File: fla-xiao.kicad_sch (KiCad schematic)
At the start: 9 parts, among them J1 Conn_PinHeader_1x08_P2.54mm_V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, J2 Conn_PinHeader_1x04_P2.54mm_V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, J3 Conn_PinHeader_2x03_P2.54mm_V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, SW1 BUTTON_B3SN, U1 MOUDLE-SEEEDUINO-XIAO-ESP32C3

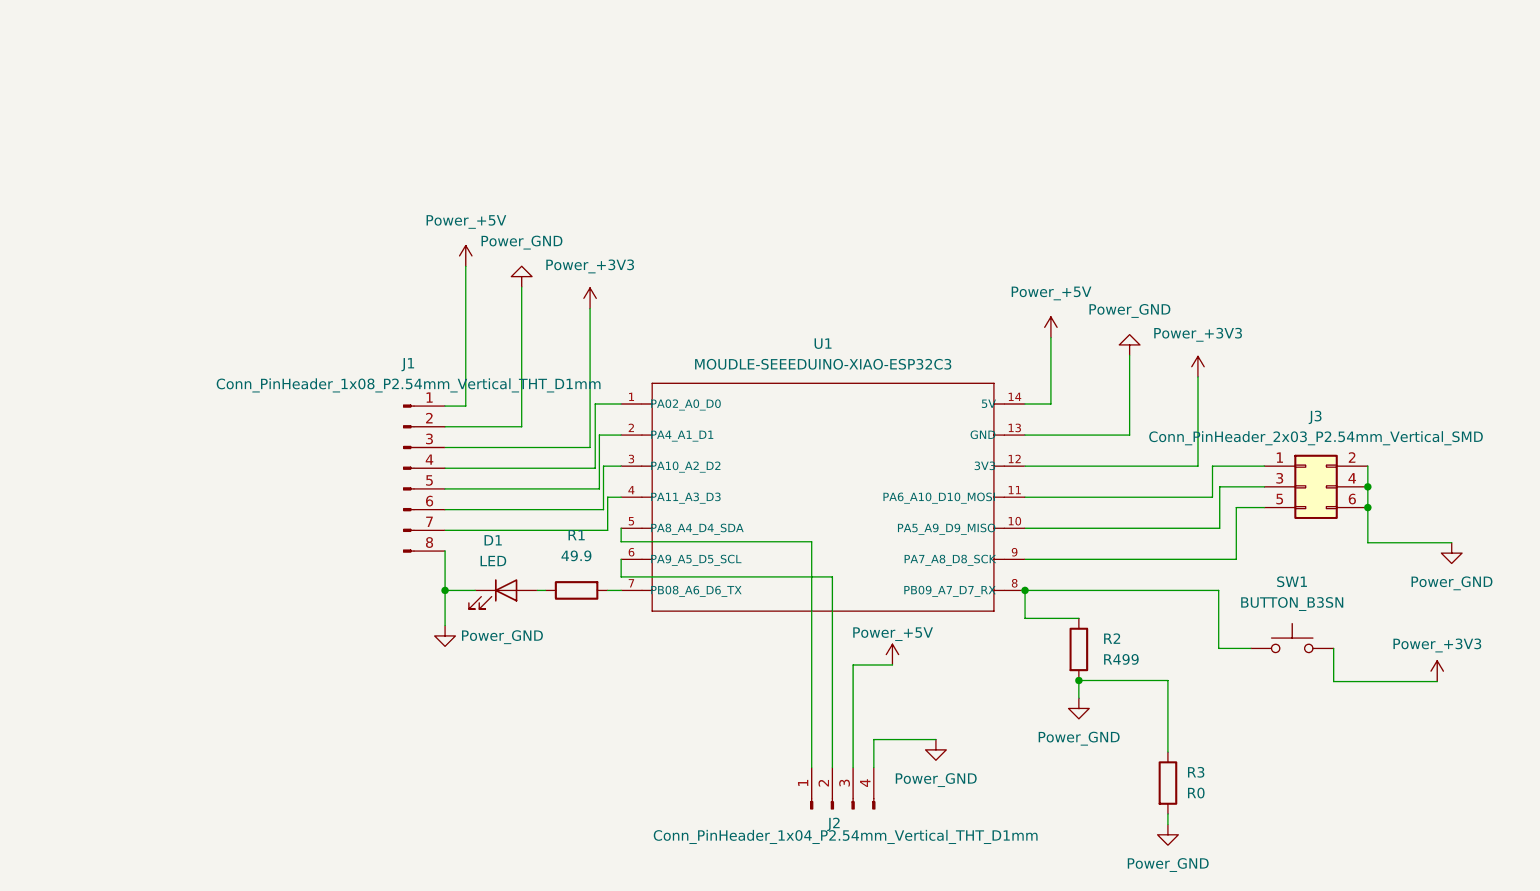
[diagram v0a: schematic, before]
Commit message: Updated to use sockets with XIAO
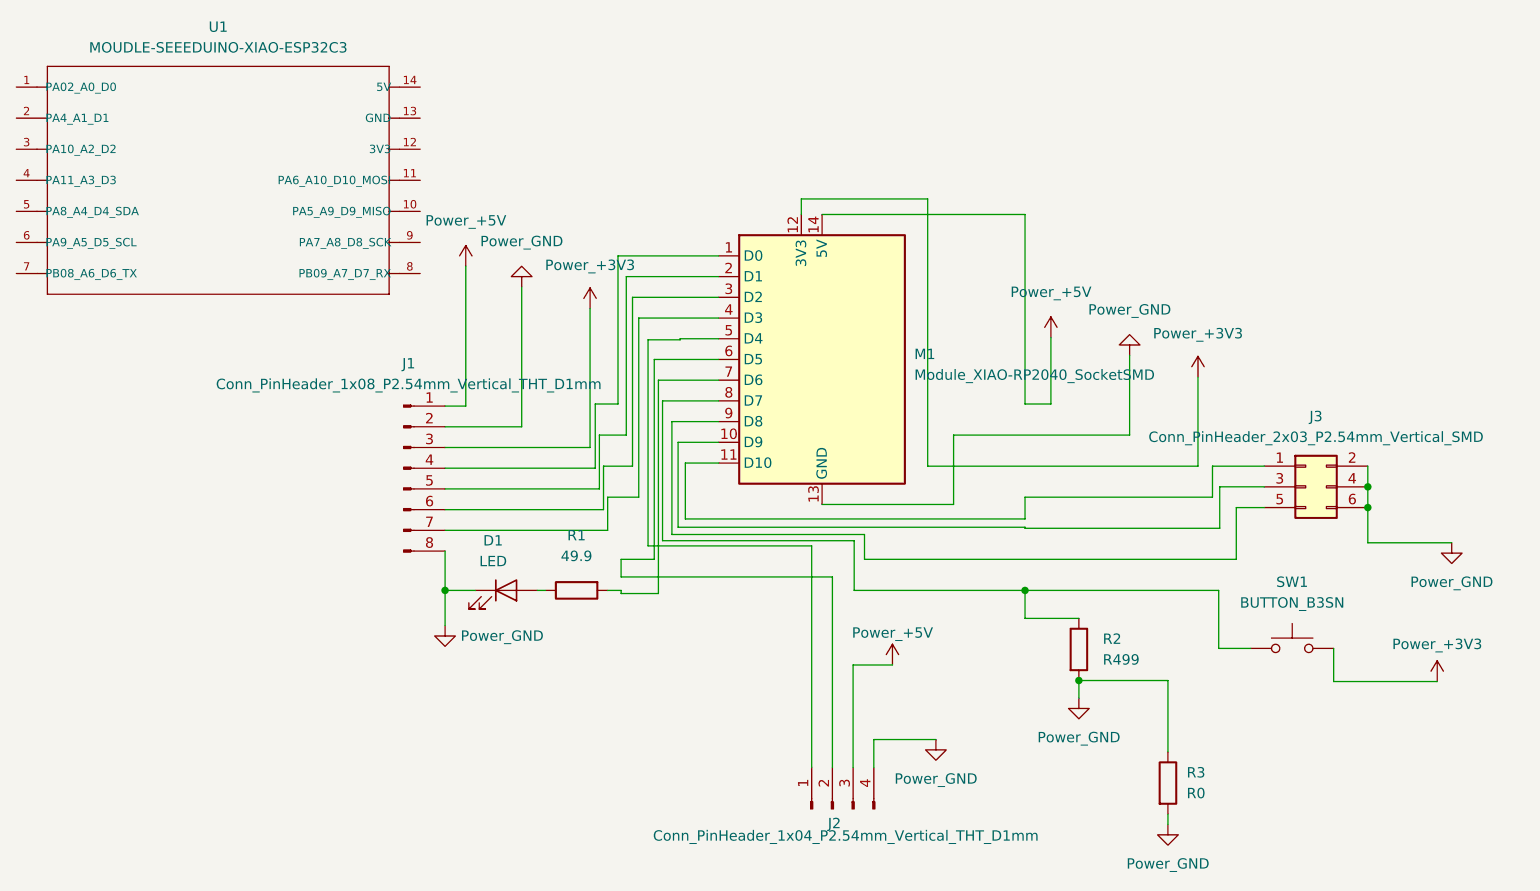
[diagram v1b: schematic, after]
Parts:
- added M1: Module_XIAO-RP2040_SocketSMD, fab:SeeedStudio_XIAO_SocketSMD, symbol fab:Module_XIAO-RP2040_SocketSMD
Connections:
- net +3V3: now also M1.12 (3V3); no longer U1.12 (3V3)
- net +5V: now also M1.14 (5V); no longer U1.14 (5V)
- net GND: now also M1.13 (GND); no longer U1.13 (GND)
- net at R2.1, SW1.1: now also M1.8 (D7); no longer U1.8 (PB09_A7_D7_RX)
- net at J1.4 (Pin_4): now also M1.1 (D0); no longer U1.1 (PA02_A0_D0)
- net at J1.5 (Pin_5): now also M1.2 (D1); no longer U1.2 (PA4_A1_D1)
- net at J1.6 (Pin_6): now also M1.3 (D2); no longer U1.3 (PA10_A2_D2)
- net at J1.7 (Pin_7): now also M1.4 (D3); no longer U1.4 (PA11_A3_D3)
- net at J3.3 (Pin_3): now also M1.10 (D9); no longer U1.10 (PA5_A9_D9_MISO)
- net at J3.1 (Pin_1): now also M1.11 (D10); no longer U1.11 (PA6_A10_D10_MOSI)
- net at J2.1 (Pin_1): now also M1.5 (D4); no longer U1.5 (PA8_A4_D4_SDA)
- net at J2.2 (Pin_2): now also M1.6 (D5); no longer U1.6 (PA9_A5_D5_SCL)
- net at R1.2: now also M1.7 (D6); no longer U1.7 (PB08_A6_D6_TX)
- net at J3.5 (Pin_5): now also M1.9 (D8); no longer U1.9 (PA7_A8_D8_SCK)

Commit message: .\fla-xiao.kicad*
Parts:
- removed U1: MOUDLE-SEEEDUINO-XIAO-ESP32C3, MOUDLE14P-SMD-2.54-21X17.8MM, symbol MOUDLE-SEEEDUINO-XIAO-ESP32C3:MOUDLE-SEEEDUINO-XIAO-ESP32C3
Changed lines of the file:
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@@
-    )
-  )
-  (symbol (lib_id "MOUDLE-SEEEDUINO-XIAO-ESP32C3:MOUDLE-SEEEDUINO-XIAO-ESP32C3") (at 64.897 37.084 0) (unit 1)
-    (in_bom yes) (on_board yes) (dnp no) (fields_autoplaced)
-    (property "Reference" "U1" (at 64.262 18.288 0)
-      (effects (font (size 1.27 1.27)))
-    )
-    (property "Value" "MOUDLE-SEEEDUINO-XIAO-ESP32C3" (at 64.262 20.828 0)
-      (effects (font (size 1.27 1.27)))
-    )
-    (property "Footprint" "MOUDLE14P-SMD-2.54-21X17.8MM" (at 64.897 37.084 0)
-      (effects (font (size 1.27 1.27)) (justify bottom) hide)
-    )
-    (property "Datasheet" "" (at 64.897 37.084 0)
-      (effects (font (size 1.27 1.27)) hide)
-    )
-    (pin "1")
-    (pin "10")
-    (pin "11")
-    (pin "12")
-    (pin "13")
-    (pin "14")
-    (pin "2")
-    (pin "3")
-    (pin "4")
-    (pin "5")
-    (pin "6")
-    (pin "7")
-    (pin "8")
-    (pin "9")
-    (instances
-      (project "fla-xiao"
-        (path "/3934cdea-42c8-4ab1-b1be-2c4978ab08ae"
-          (reference "U1") (unit 1)
-        )
-      )
     )
   )
